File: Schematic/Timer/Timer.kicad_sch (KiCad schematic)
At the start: 51 parts, among them J1 DC Input 19V, J2 Output, J3 SWDIO+Serial, Q1 SI7145, Q2 SI7145, Q3 BSS138, SW1 RESET, SW2 PEC11R-4020F-S0012, U1 STM32F103CBT, U2 TPS54302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

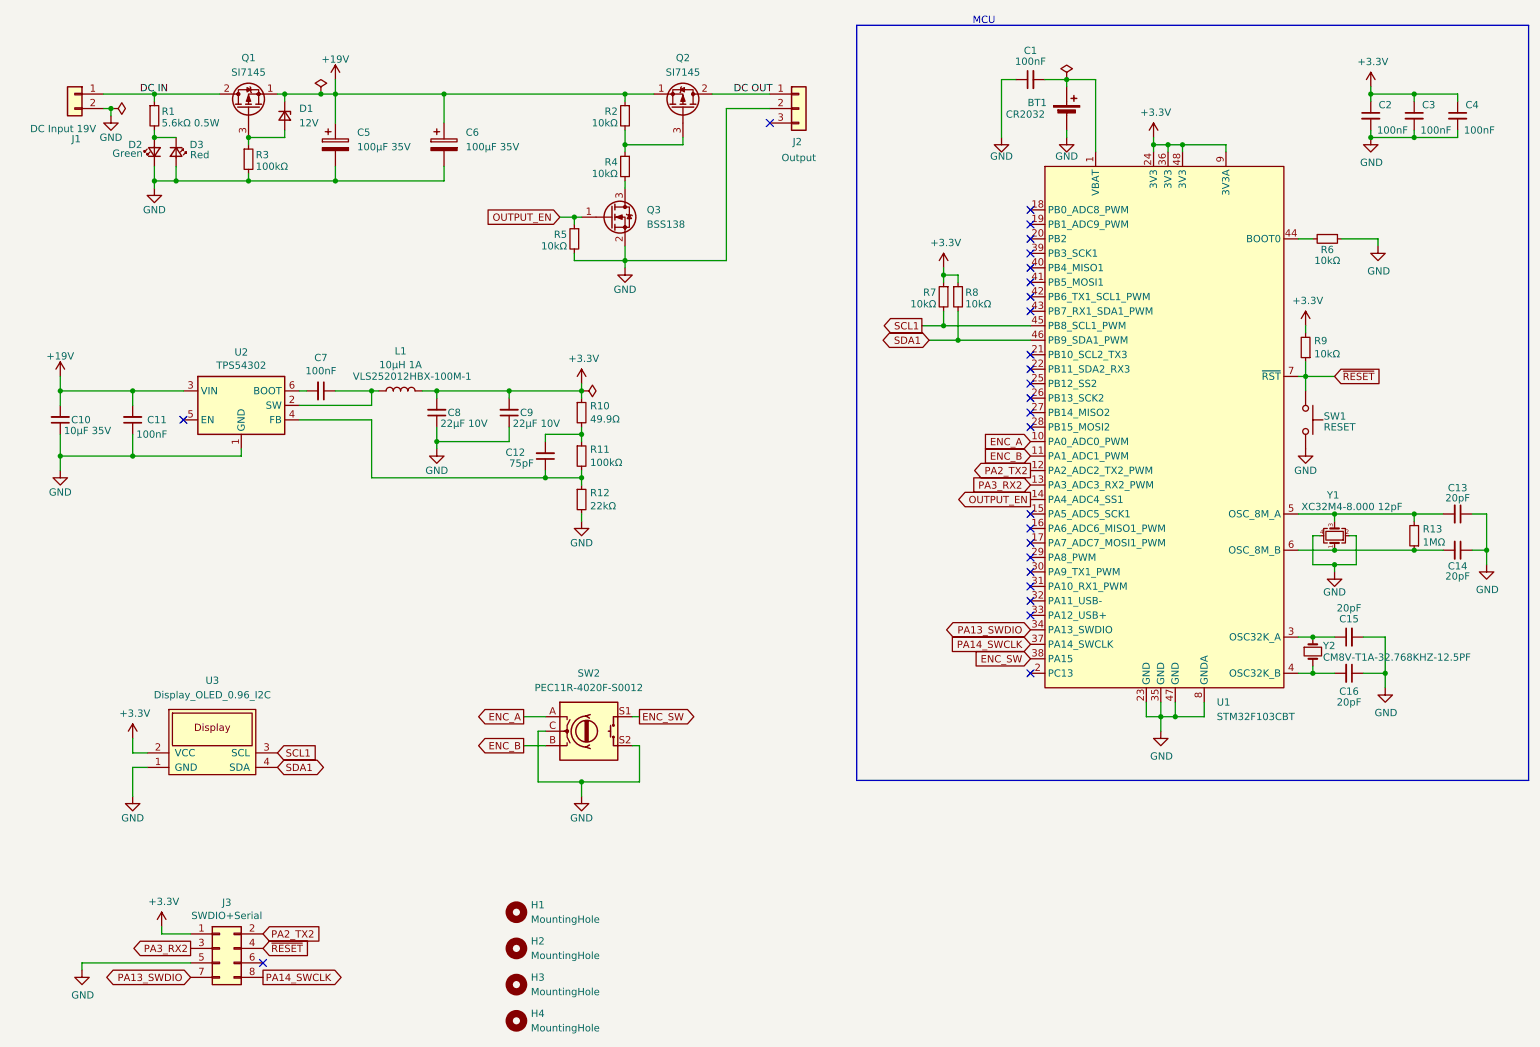
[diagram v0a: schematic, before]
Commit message: Rearranged schematic, added copy ring
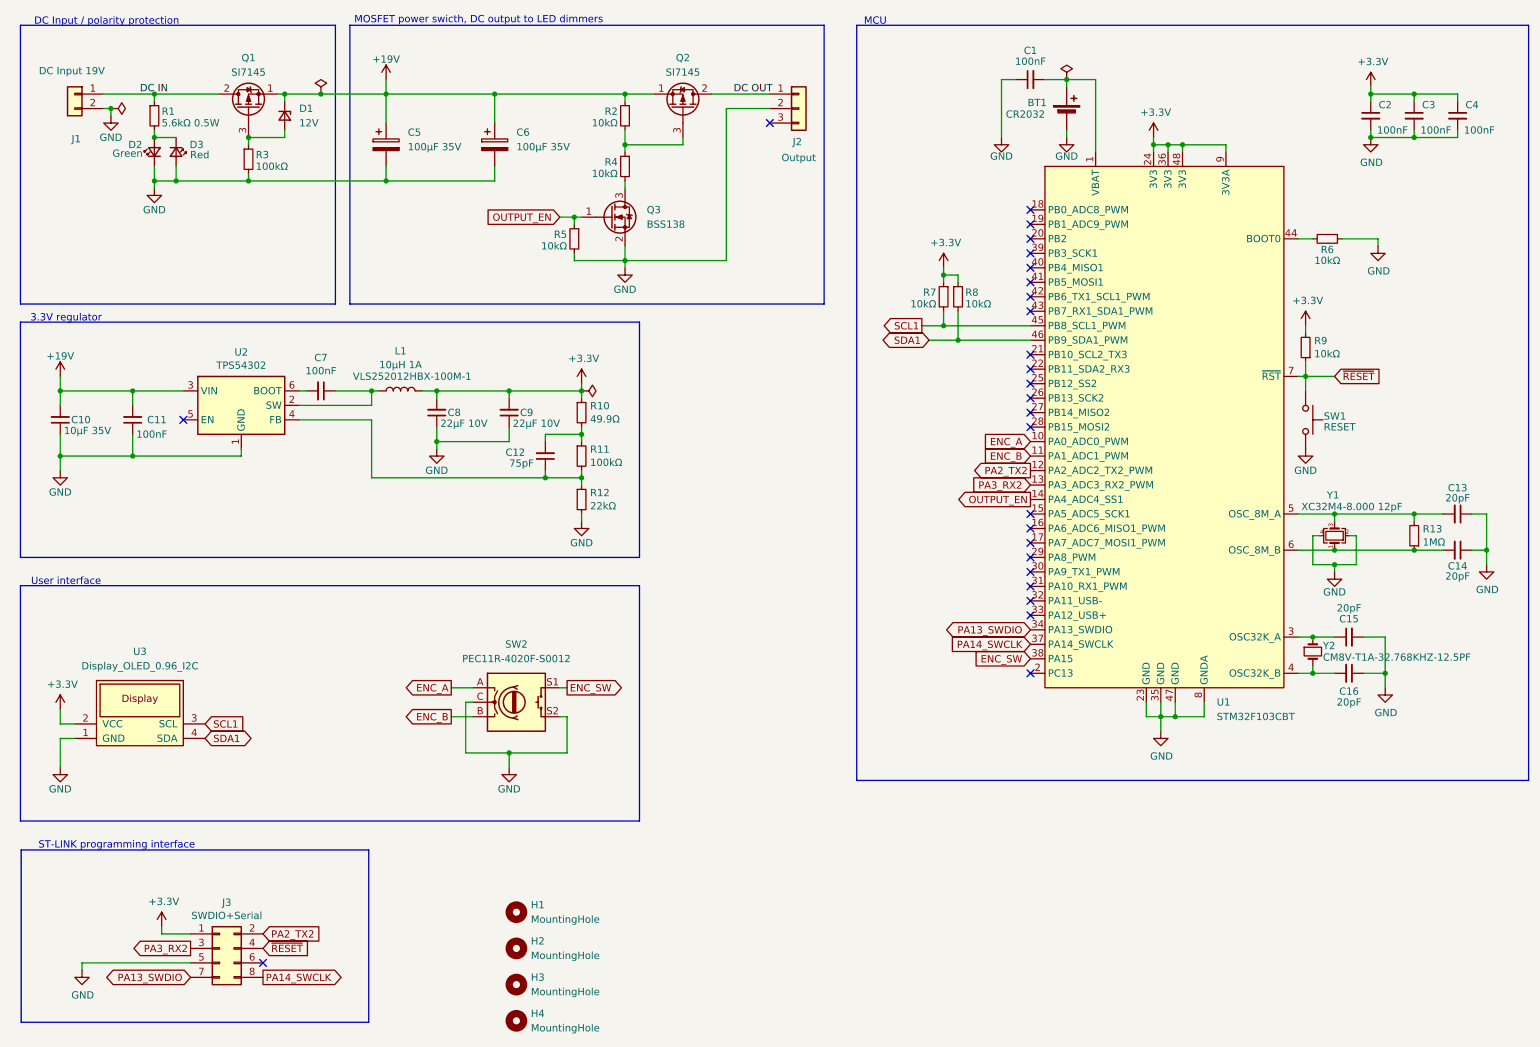
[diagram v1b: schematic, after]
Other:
- note added: "3.3V regulator"
- note added: "DC Input / polarity protection"
- note added: "MOSFET power swicth, DC output to LED dimmers"
- note added: "ST-LINK programming interface"
- note added: "User interface"
- moved on the sheet: C5, C6, SW2, U3
